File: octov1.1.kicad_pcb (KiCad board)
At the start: 2 copper layers, 60 x 95.6 mm, 84 parts, among them J1 Conn_01x02, J10 SERVO3_CONN, J11 SWITCH4_CONN, J12 SERVO4_CONN, J13 SWITCH5_CONN, J14 SERVO5_CONN, J15 USB_C_Receptacle_USB2.0_14P, J16 SERVO1_CONN, J2 SERVO0_CONN, J3 SWITCH0_CONN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

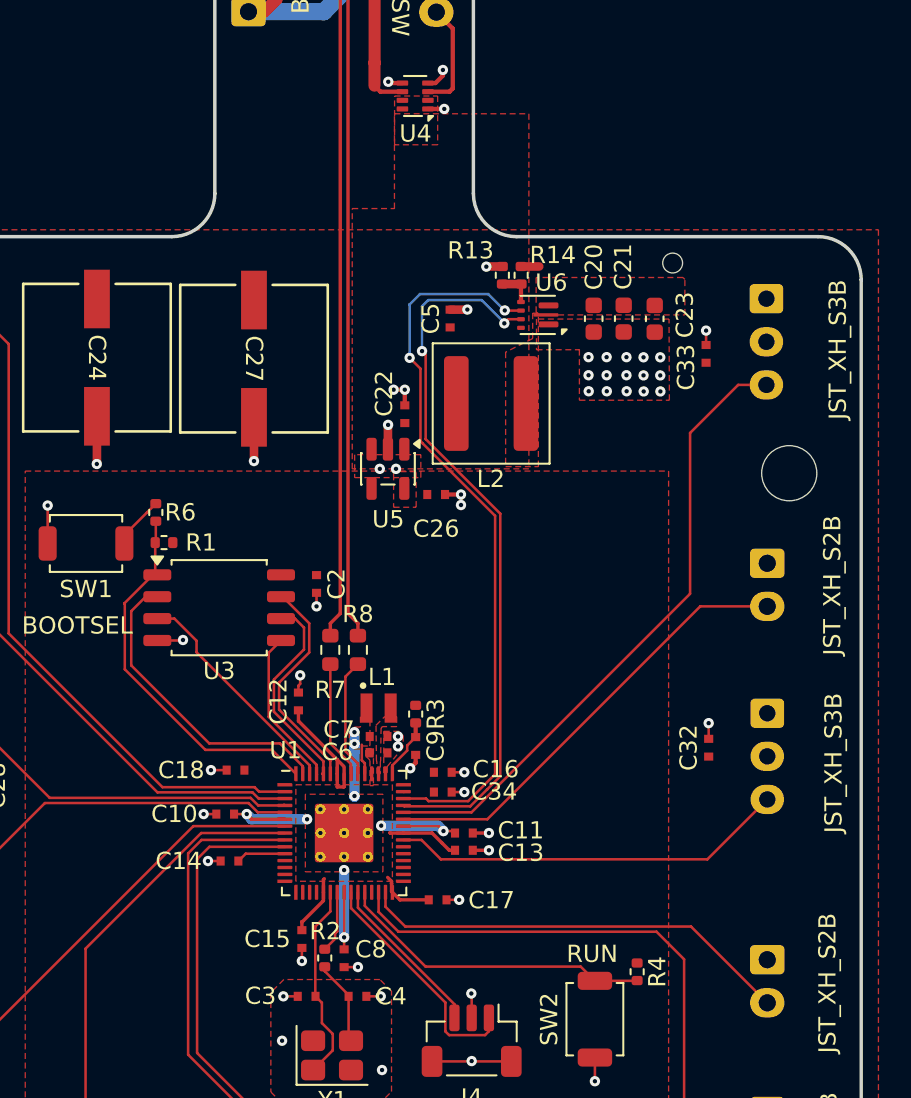
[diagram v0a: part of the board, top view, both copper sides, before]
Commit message: Add testpoints
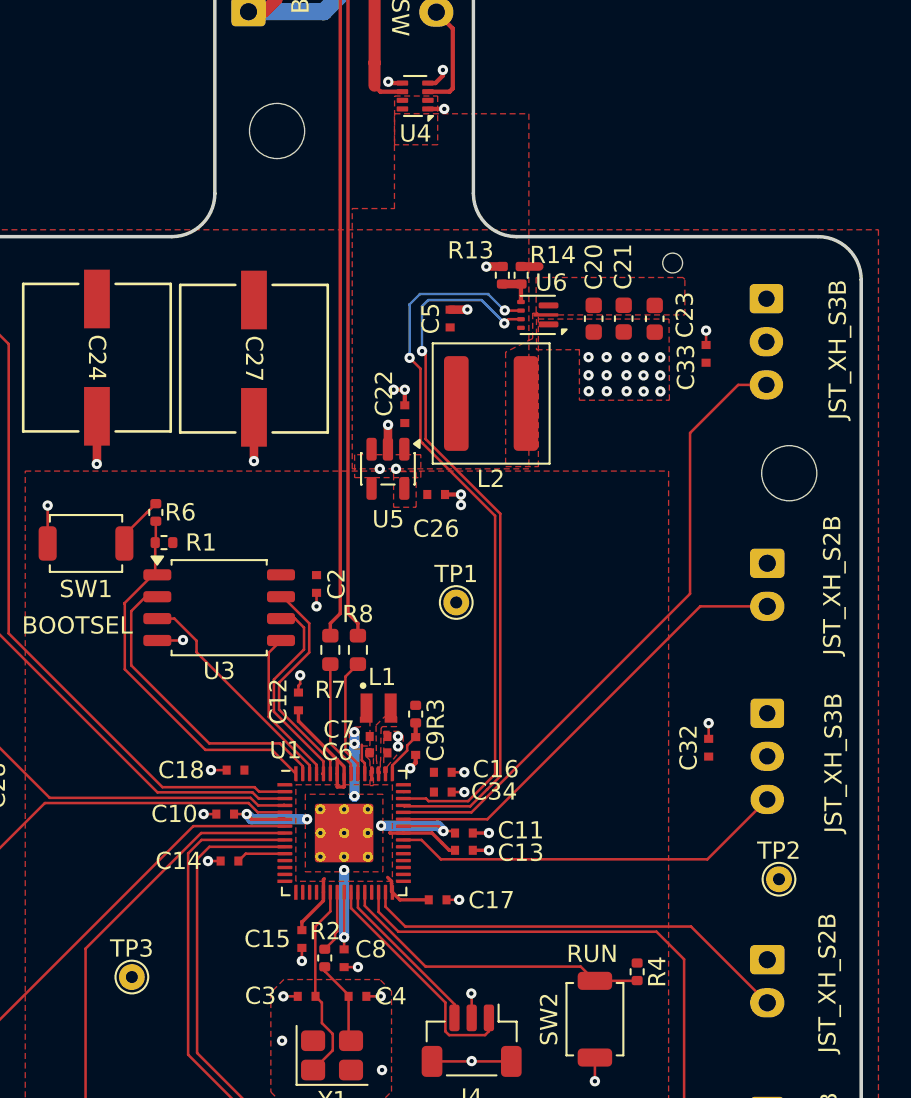
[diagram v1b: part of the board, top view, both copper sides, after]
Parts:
- added REF**: MountingHole_3.2mm_M3, MountingHole:MountingHole_3.2mm_M3, F.Cu at (96.1, 59.3)
- added TP1: TestPoint, TestPoint:TestPoint_THTPad_D1.5mm_Drill0.7mm, F.Cu at (106.5, 86.6)
- added TP2: TestPoint, TestPoint:TestPoint_THTPad_D1.5mm_Drill0.7mm, F.Cu at (125.2, 102.7)
- added TP3: TestPoint, TestPoint:TestPoint_THTPad_D1.5mm_Drill0.7mm, F.Cu at (87.7, 108.4)

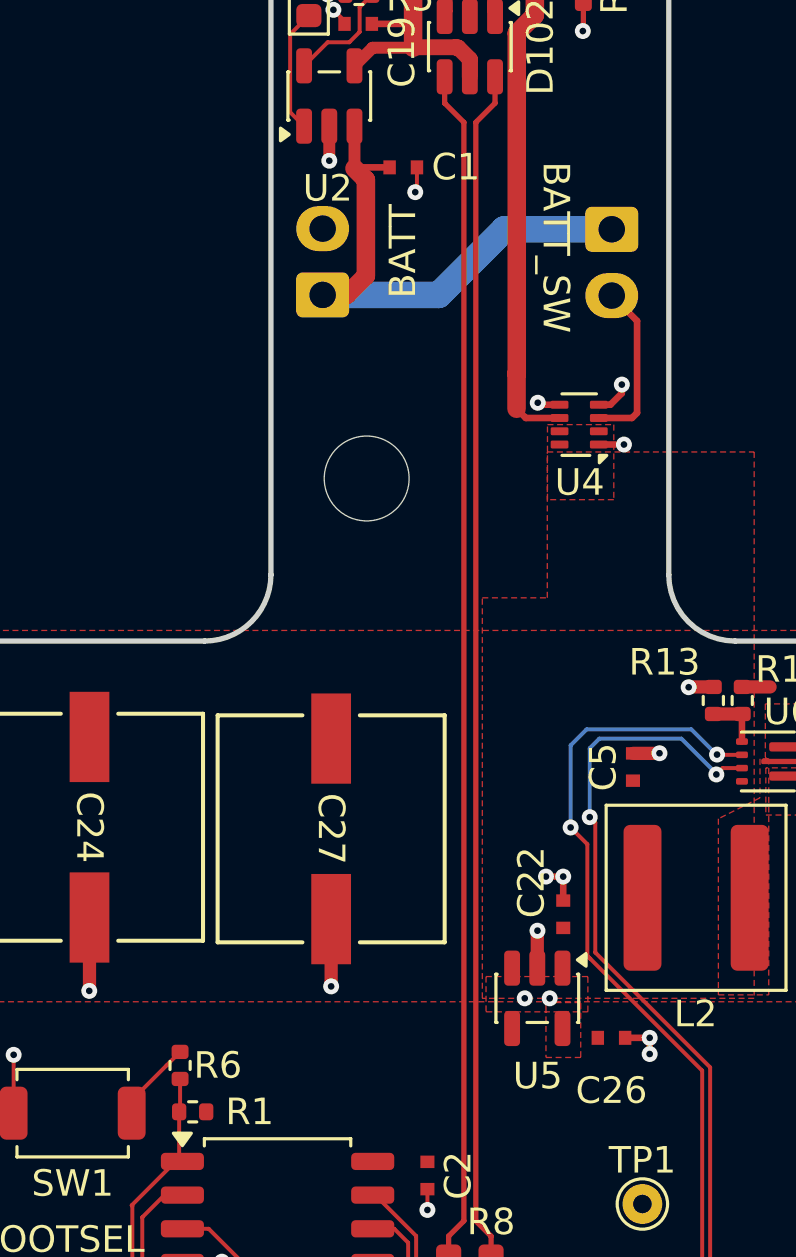
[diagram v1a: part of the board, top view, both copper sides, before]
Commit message: Fix some bugs in the circuit
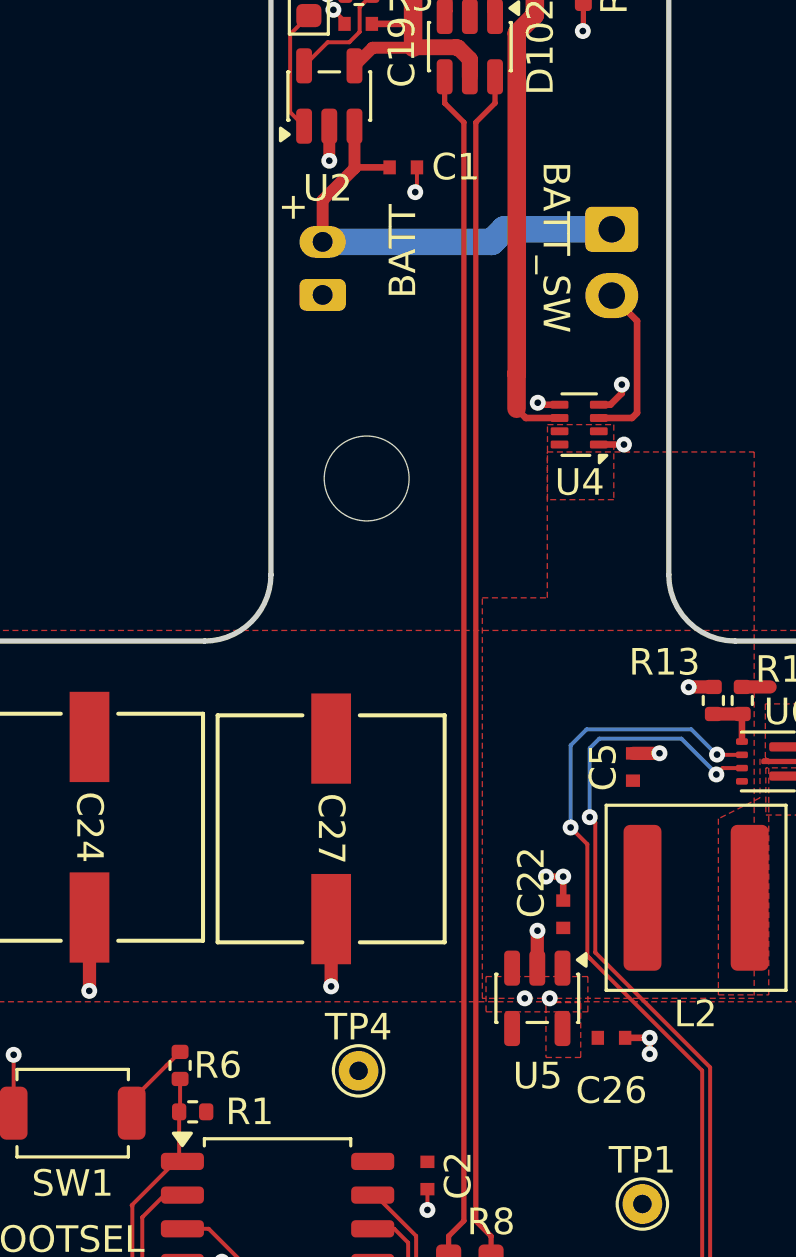
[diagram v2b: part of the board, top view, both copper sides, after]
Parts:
- added TP4: TestPoint, TestPoint:TestPoint_THTPad_D1.5mm_Drill0.7mm, F.Cu at (95.8, 81.6)
- C24, C27: value C_Polarized -> 470u
- J1: footprint Connector_JST:JST_XH_S2B-XH-A-1_1x02_P2.50mm_Horizontal -> Connector_JST:JST_PH_S2B-PH-K_1x02_P2.00mm_Horizontal
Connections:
- J1 pad 1: /Power System/V_BAT -> GND
- J1 pad 2: GND -> /Power System/V_BAT
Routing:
- net /Power System/V_BAT: track 21.0 -> 17.4 mm
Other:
- board text added: "+"
